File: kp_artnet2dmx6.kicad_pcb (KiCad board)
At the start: 2 copper layers, 108 parts, among them IC1 KSZ8081MNXIA-TR, IC2 M95640-RMN6P, IC3 AP2281-3WG-7, IC4 MP2331HGTL-P, J1 RJ45_Amphenol_RJMG1BD3B8K1ANR, J10 DMX, J11 DMX, J12 DMX, J14 SWD, J15 USB-B-S-RA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

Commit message: start assigning netclasses
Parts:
- IC4: footprint SamacSys:MP2331HGTLP -> Package_TO_SOT_SMD:SOT-583-8
- U1: value STM32F407VETx -> STM32F407VGT6
- moved SW1 109.0 mm to (131.7, 112.3), turned to -90 degrees
- moved R1 100.9 mm to (126.8, 113.0), turned to 0 degrees
- moved R29 87.9 mm to (121.0, 111.1), turned to -90 degrees
- moved R30 83.3 mm to (118.5, 111.1), turned to -90 degrees
- moved J14 81.6 mm to (117.6, 117.2), turned to 90 degrees
- moved R31 78.8 mm to (115.9, 111.1), turned to -90 degrees
- moved R32 74.9 mm to (113.6, 111.1), turned to -90 degrees
- moved R21 72.5 mm to (98.5, 94.8), turned to 90 degrees
- moved C3 67.7 mm to (99.5, 90.7), turned to -90 degrees
- moved C4 59.1 mm to (103.3, 74.6), turned to 0 degrees
- moved C9 58.1 mm to (103.1, 72.6), turned to 0 degrees
- moved C5 52.8 mm to (88.5, 90.7), turned to -90 degrees
- moved R19 50.5 mm to (107.3, 56.5)
- moved C21 50.5 mm to (106.5, 61.0)
- moved IC2 50.5 mm to (102.6, 58.3)
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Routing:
- added copper zone on In2.Cu, net +3.3V
- added copper zone on In2.Cu, net +5V
- added copper zone on In2.Cu, net +5V_IN
- added copper zone on B.Cu, net GND
- added copper zone on F.Cu, net GND
- added copper zone on In1.Cu, net GND
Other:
- board outline added: 84 x 104 mm
- copper layers 2 -> 4
- rule pad_to_mask_clearance: 0 -> 0.05

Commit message: main pcb : everything is connected
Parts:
- moved R21 31.7 mm to (99.4, 63.2), turned to 0 degrees
- moved R30 14.8 mm to (104.5, 115.8), turned to 90 degrees
- moved R29 14.8 mm to (107.0, 115.8), turned to 90 degrees
- moved R31 14.8 mm to (101.9, 115.8), turned to 90 degrees
- moved R32 14.8 mm to (99.7, 115.9), turned to 90 degrees
- moved J14 14.4 mm to (103.3, 116.0)
- moved R25 13.4 mm to (77.9, 35.0), turned to -45 degrees
- moved R24 11.6 mm to (75.4, 37.6), turned to -45 degrees
- moved C14 11.0 mm to (69.2, 83.2)
- moved D1 11.0 mm to (72.1, 81.7)
- moved R7 11.0 mm to (72.3, 83.2)
- moved R14 9.23 mm to (94.3, 102.9), turned to -45 degrees
- moved R19 8.43 mm to (99.1, 54.5)
- moved R13 8.07 mm to (93.1, 104.1), turned to -45 degrees
- moved C21 7.74 mm to (99.0, 59.1)
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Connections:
- net Net-(C38-Pad1) renamed /mp2331_fb2
- net Net-(C39-Pad2) renamed /mp2331_bst2
- net Net-(IC1-REXT) renamed /ksz_rext
- net Net-(IC4-BST) renamed /mp2331_bst1
- net Net-(IC4-EN) renamed /mp2331_en
- net Net-(IC4-FB) renamed /mp2331_fb1
- net Net-(IC4-PG) renamed /mp2331_pg
- net Net-(IC4-SS) renamed /mp2331_ss
- net Net-(J1-PadL1) renamed /ksz_led0+
- net Net-(J1-PadL4) renamed /ksz_led1+
- net Net-(J1-RCT) renamed /rj45_tct
- net Net-(J1-TCT) renamed /rj45_rct
- net Net-(J14-Pin_10) renamed /swd_nrst
- net Net-(J14-Pin_2) renamed /swd_io
- net Net-(J14-Pin_4) renamed /swd_clk
- net Net-(J14-Pin_6) renamed /swd_swo
- net Net-(Q1-D) renamed /usbmos1
- net Net-(Q1-S) renamed /usbmos2
- net Net-(SW1-B) renamed /bootswitch
- J1 pad R8: Earth -> GND
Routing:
- net GND: track 0.00 -> 107.1 mm, vias 0 -> 46
- net STM_NRST: track 0.00 -> 105.9 mm, vias 0 -> 6
- net +3.3V: track 0.00 -> 89.9 mm, vias 0 -> 27
- net STM_SPI2_MISO: track 0.00 -> 82.0 mm, vias 0 -> 2
- net STM_SPI2_SCK: track 0.00 -> 80.6 mm, vias 0 -> 2
- net STM_SPI2_MOSI: track 0.00 -> 76.8 mm, vias 0 -> 3
- net STM_BOOT0: track 0.00 -> 72.7 mm
- net STM_PWR_5V_EN_GPIO: track 0.00 -> 69.0 mm, vias 0 -> 2
- net STM_USB_D-: track 0.00 -> 68.0 mm, vias 0 -> 2
- net STM_SWO: track 0.00 -> 67.7 mm, vias 0 -> 2
- net STM_USB_D+: track 0.00 -> 67.4 mm, vias 0 -> 2
- net STM_MCP_RESET_GPIO: track 0.00 -> 65.6 mm, vias 0 -> 1
- net STM_MCP_INTB_GPIO: track 0.00 -> 63.1 mm, vias 0 -> 1
- net STM_I2C1_SCL: track 0.00 -> 62.6 mm, vias 0 -> 2
- net STM_I2C1_SDA: track 0.00 -> 59.8 mm, vias 0 -> 2
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- added copper zone on In2.Cu, net +5V_USB
- added copper zone on B.Cu, net Earth
- added copper zone on F.Cu, net Earth

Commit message: fix drc errors
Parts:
- removed TP1: testpoint, TestPoint:TestPoint_THTPad_1.5x1.5mm_Drill0.7mm
- moved R10 2.12 mm to (76.8, 111.2)
- moved R11 2.12 mm to (78.5, 111.2)
- moved R2 2.12 mm to (72.0, 111.2)
- moved R3 2.12 mm to (70.2, 111.3)
- moved R8 2.12 mm to (73.7, 111.2)
- moved R9 2.12 mm to (75.2, 111.2)
- moved C5 0.57 mm to (88.7, 90.2), turned to 180 degrees
- moved C16 0.25 mm to (81.3, 104.6)
- moved C17 0.25 mm to (79.7, 103.0)
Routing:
- net STM_SPI2_NSS2_GPIO: track 0.00 -> 102.1 mm, vias 0 -> 3
- net STM_ETH_TX_EN: track 0.00 -> 27.2 mm, vias 0 -> 2
- net GND: track 107.1 -> 114.9 mm, vias 46 -> 50
- net STM_ETH_RXD3: track 36.8 -> 42.3 mm
- net STM_ETH_RXD2: track 33.9 -> 39.1 mm
- net STM_ETH_RXD0: track 29.6 -> 34.0 mm
- net STM_ETH_RXD1: track 33.8 -> 36.0 mm
- net /ksz_rext: track 7.65 -> 9.77 mm
- net STM_ETH_MDIO: track 41.8 -> 43.8 mm
- net MCP_B4: track 25.6 -> 24.9 mm
- net MCP_B7: track 25.4 -> 24.8 mm
- net STM_ETH_TXD0: track 33.5 -> 34.1 mm
- net +3.3V: track 89.9 -> 90.2 mm, vias 27 -> 28
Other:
- outline, holes or cut-outs redrawn

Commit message: schematic: change connectors from jst xh to IDC
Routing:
- net GND: vias 50 -> 70
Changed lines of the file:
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@@
 	)
 	(via
+		(at 62 42)
+		(size 0.8)
+		(drill 0.25)
+		(layers "F.Cu" "B.Cu")
+		(net "GND")
+	)
+	(via
 		(at 80.55 73.95)
 		(size 0.8)
@@
 	)
 	(via
+		(at 60.5 33.5)
+		(size 0.8)
+		(drill 0.25)
+		(layers "F.Cu" "B.Cu")
+		(net "GND")
+	)
+	(via
+		(at 84 33.5)
+		(size 0.8)
+		(drill 0.25)
+		(layers "F.Cu" "B.Cu")
+		(net "GND")
+	)
+	(via
 		(at 105.55 72.65)
 		(size 0.8)
@@
 	)
 	(via
+		(at 88.5 113.5)
+		(size 0.8)
+		(drill 0.25)
+		(layers "F.Cu" "B.Cu")
+		(net "GND")
+	)
+	(via
+		(at 102.5 100)
+		(size 0.8)
+		(drill 0.25)
+		(layers "F.Cu" "B.Cu")
+		(net "GND")
+	)
+	(via
 		(at 91.4 107.35)
 		(size 0.8)
@@
 	)
 	(via
+		(at 129 39)
+		(size 0.8)
+		(drill 0.25)
+		(layers "F.Cu" "B.Cu")
+		(net "GND")
+	)
+	(via
 		(at 103.25 75.5)
 		(size 0.8)
@@
 	)
 	(via
+		(at 67.5 63.5)
+		(size 0.8)
+		(drill 0.25)
+		(layers "F.Cu" "B.Cu")
+		(net "GND")
+	)
+	(via
 		(at 80.6 80.3)
 		(size 0.8)
@@
 	)
 	(via
+		(at 94.5 123)
+		(size 0.8)
+		(drill 0.25)
+		(layers "F.Cu" "B.Cu")
+		(net "GND")
+	)
+	(via
 		(at 68.15 112.225)
 		(size 0.8)
@@
 	)
 	(via
+		(at 81 123)
+		(size 0.8)
+		(drill 0.25)
+		(layers "F.Cu" "B.Cu")
+		(net "GND")
+	)
+	(via
+		(at 68.5 123)
+		(size 0.8)
+		(drill 0.25)
+		(layers "F.Cu" "B.Cu")
+		(net "GND")
+	)
+	(via
 		(at 105.3 74.65)
 		(size 0.8)
@@
 	)
 	(via
+		(at 72 72.5)
+		(size 0.8)
+		(drill 0.25)
+		(layers "F.Cu" "B.Cu")
+		(net "GND")
+	)
+	(via
 		(at 104.53 111.99)
 		(size 0.8)
@@
 	)
 	(via
+		(at 64 72.5)
+		(size 0.8)
+		(drill 0.25)
+		(layers "F.Cu" "B.Cu")
+		(net "GND")
+	)
+	(via
 		(at 82.5 49.65)
 		(size 0.8)
@@
 	)
 	(via
+		(at 121 116.5)
+		(size 0.8)
+		(drill 0.25)
+		(layers "F.Cu" "B.Cu")
+		(net "GND")
+	)
+	(via
+		(at 87 63)
+		(size 0.8)
+		(drill 0.25)
+		(layers "F.Cu" "B.Cu")
+		(net "GND")
+	)
+	(via
 		(at 79.6 104.65)
 		(size 0.8)
@@
 	)
 	(via
+		(at 79.5 44)
+		(size 0.8)
+		(drill 0.25)
+		(layers "F.Cu" "B.Cu")
+		(net "GND")
+	)
+	(via
+		(at 107 61)
+		(size 0.8)
+		(drill 0.25)
+		(layers "F.Cu" "B.Cu")
+		(net "GND")
+	)
+	(via
 		(at 82.2 87.4)
 		(size 0.8)
@@
 	)
 	(via
+		(at 112 99)
+		(size 0.8)
+		(drill 0.25)
+		(layers "F.Cu" "B.Cu")
+		(net "GND")
+	)
+	(via
 		(at 76.65 101.2)
 		(size 0.8)
@@
 	)
 	(via
+		(at 106 54)
+		(size 0.8)
+		(drill 0.25)
+		(layers "F.Cu" "B.Cu")
+		(net "GND")
+	)
+	(via
 		(at 59.5 99.25)
 		(size 0.8)
@@
 	)
 	(via
+		(at 64 83)
+		(size 0.8)
+		(drill 0.25)
+		(layers "F.Cu" "B.Cu")
+		(net "GND")
+	)
+	(via
 		(at 88.374694 86.224694)
 		(size 0.8)
@@
 	)
 	(via
+		(at 115 122.5)
+		(size 0.8)
+		(drill 0.25)
+		(layers "F.Cu" "B.Cu")
+		(net "GND")
+	)
+	(via
 		(at 100.63 111.79)
 		(size 0.8)
@@
 		)
 		(min_thickness 0.25)
-		(fill yes
+		(fill
 			(thermal_gap 0.5)
 			(thermal_bridge_width 0.5)
@@
 		)
 		(min_thickness 0.25)
-		(fill yes
+		(fill
 			(thermal_gap 0.5)
 			(thermal_bridge_width 0.5)
@@
 		)
 		(min_thickness 0.25)
-		(fill yes
+		(fill
 			(thermal_gap 0.5)
 			(thermal_bridge_width 0.5)
@@
 		)
 		(min_thickness 0.25)
-		(fill yes
+		(fill
 			(thermal_gap 0.5)
 			(thermal_bridge_width 0.5)
@@
 		)
 		(min_thickness 0.25)
-		(fill yes
+		(fill
 			(thermal_gap 0.5)
 			(thermal_bridge_width 0.5)
@@
 		)
 		(min_thickness 0.25)
-		(fill yes
+		(fill
 			(thermal_gap 0.5)
 			(thermal_bridge_width 0.5)
@@
 		)
 		(min_thickness 0.25)
-		(fill yes
+		(fill
 			(thermal_gap 0.5)
 			(thermal_bridge_width 0.5)
@@
 		)
 		(min_thickness 0.25)
-		(fill yes
+		(fill
 			(thermal_gap 0.5)
 			(thermal_bridge_width 0.5)
@@
 		)
 		(min_thickness 0.25)
-		(fill yes
+		(fill
 			(thermal_gap 0.5)
 			(thermal_bridge_width 0.5)
@@
 		)
 		(min_thickness 0.25)
-		(fill yes
+		(fill
 			(thermal_gap 0.5)
 			(thermal_bridge_width 0.5)
@@
 		)
 		(min_thickness 0.25)
-		(fill yes
+		(fill
 			(thermal_gap 0.5)
 			(thermal_bridge_width 0.5)

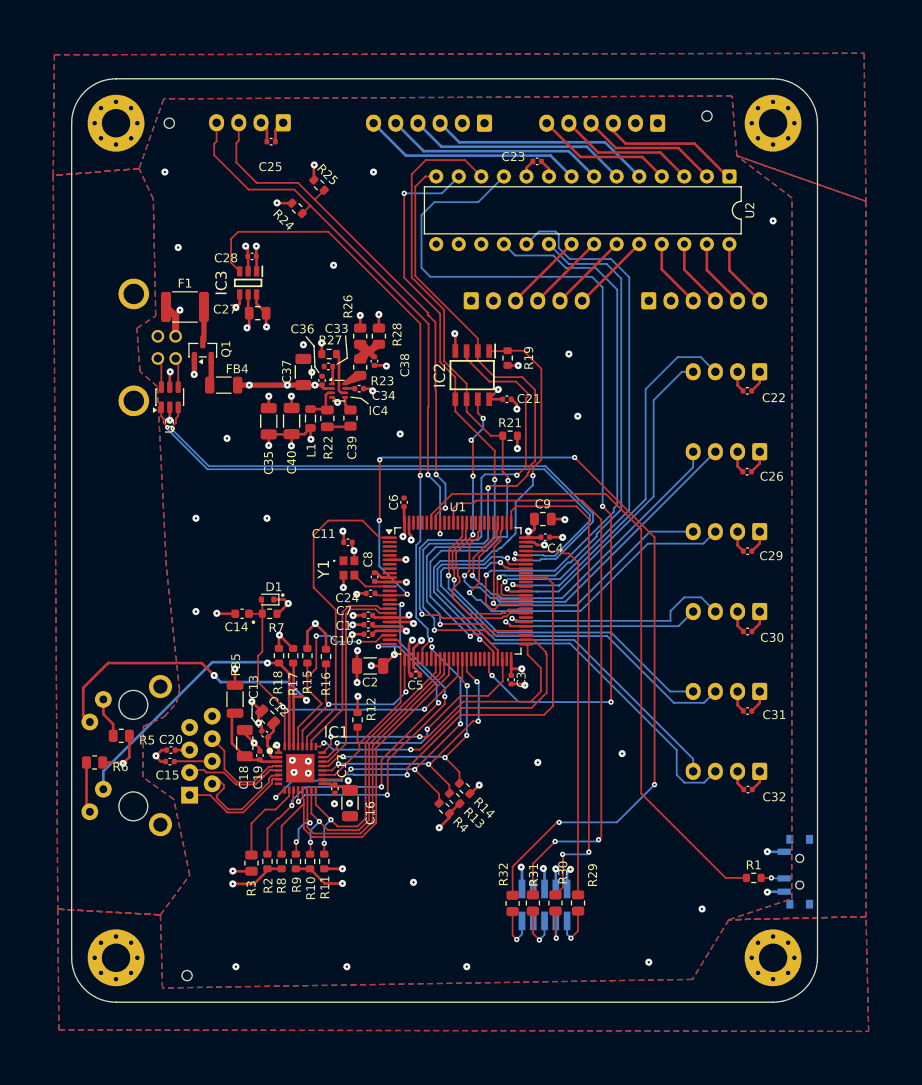
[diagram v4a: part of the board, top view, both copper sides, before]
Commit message: pcb: change connectors to IDC
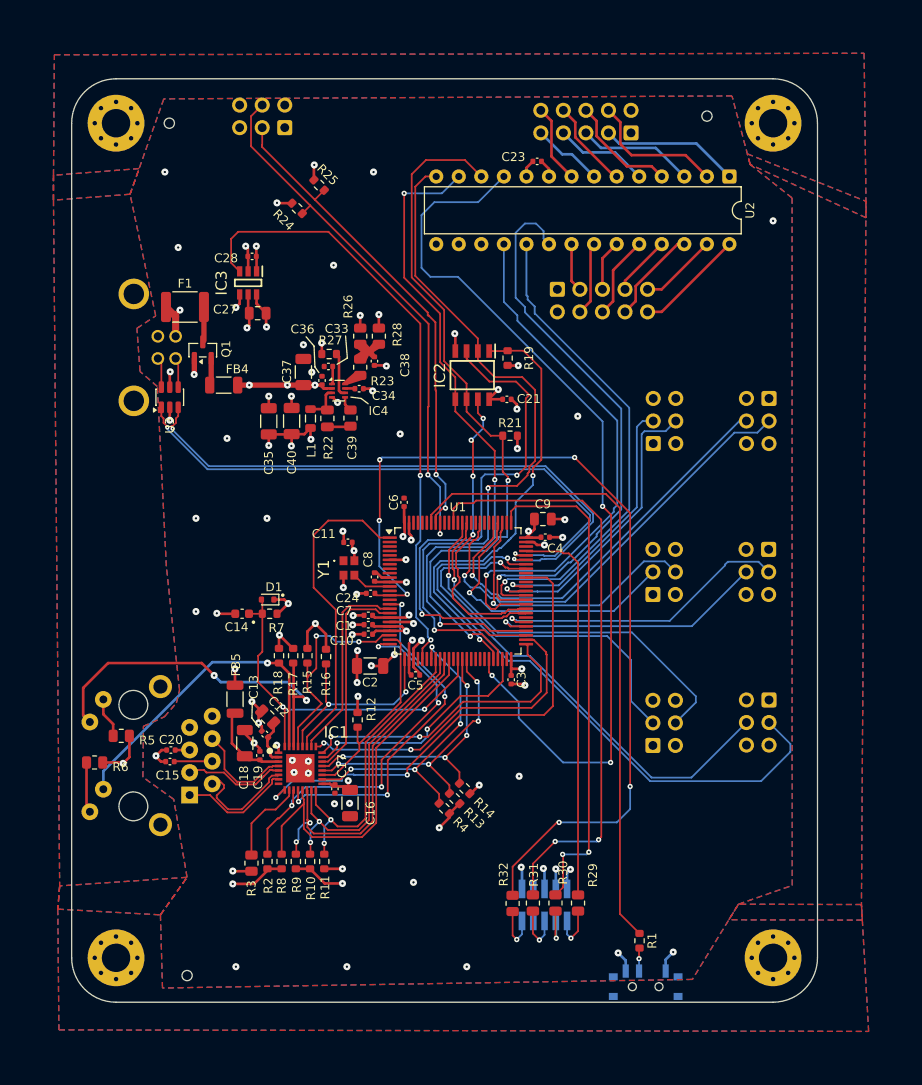
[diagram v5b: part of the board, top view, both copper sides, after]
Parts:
- removed C22, C25, C26, C29, C30, C31, C32: 100n, Capacitor_SMD:C_0402_1005Metric
- removed J4, J6: BTN, Connector_JST:JST_XH_B6B-XH-A_1x06_P2.50mm_Vertical
- J10, J11, J12, J2, J7, J8, J9: footprint Connector_JST:JST_XH_B4B-XH-A_1x04_P2.50mm_Vertical -> Connector_IDC:IDC-Header_2x03_P2.54mm_Vertical
- J3, J5: footprint Connector_JST:JST_XH_B6B-XH-A_1x06_P2.50mm_Vertical -> Connector_IDC:IDC-Header_2x05_P2.54mm_Vertical
- moved SW1 21.2 mm to (114.7, 124.9), turned to 180 degrees
- moved R1 14.7 mm to (114.0, 120.1), turned to -90 degrees
- moved J12 14.5 mm to (115.5, 64.1), turned to 0 degrees
- moved J10 14.0 mm to (115.5, 81.1), turned to 0 degrees
- moved J8 13.5 mm to (115.5, 98.1), turned to 0 degrees
- moved J5 9.79 mm to (104.7, 46.7), turned to -90 degrees
- moved J7 8.11 mm to (128.5, 93.0)
- moved J9 7.07 mm to (128.5, 76.0)
- moved J11 6.09 mm to (128.5, 59.0)
- moved J3 3.19 mm to (113.0, 29.1), turned to 90 degrees
- moved J2 0.58 mm to (74.0, 28.5), turned to 90 degrees
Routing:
- net GND: track 114.9 -> 97.7 mm, vias 70 -> 66
- net +5V: track 23.4 -> 6.24 mm
- net MCP_B6: track 24.8 -> 8.03 mm
- net MCP_B7: track 24.8 -> 8.88 mm
- net MCP_B5: track 24.9 -> 10.1 mm
- net MCP_B4: track 24.9 -> 10.6 mm
- net STM_USART6_RX: track 43.1 -> 30.4 mm
- net STM_USART1_RX: track 56.0 -> 67.8 mm
- net STM_UART4_RX: track 41.4 -> 32.5 mm
- net STM_USART1_TX: track 49.9 -> 58.0 mm
- net STM_USART3_TX: track 24.5 -> 32.3 mm
- net STM_UART5_RX: track 43.7 -> 51.2 mm
- net STM_USART3_RX: track 27.2 -> 34.0 mm
- net STM_MCP_INTB_GPIO: track 63.1 -> 56.5 mm
- net STM_UART5_TX: track 40.7 -> 47.1 mm
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
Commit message: dmxinout: do board
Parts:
- added G***: LOGO, homemade_footprints:pxm_testlogo_v1, F.Cu at (120.2, 111.3)
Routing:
- net +5V_IN: vias 6 -> 7
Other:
- board text added: "JLCJLCJLCJLC"
- board text added: "artnet2dmx6_00"

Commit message: main board : start doing sig gnd gnd sigpow
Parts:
- IC4: footprint Package_TO_SOT_SMD:SOT-583-8 -> SamacSys:MP2331HGTLP
- moved U2 70.8 mm to (130.3, 104.5), turned to 180 degrees
- moved J8 69.3 mm to (89.0, 34.0)
- moved J5 64.7 mm to (140.0, 100.9), turned to 180 degrees
- moved J3 59.7 mm to (137.5, 83.5), turned to 0 degrees
- moved C23 58.6 mm to (132.2, 82.8), turned to 90 degrees
- moved J10 48.7 mm to (103.0, 34.0)
- moved IC2 46.1 mm to (115.7, 97.7), turned to 90 degrees
- moved R19 44.0 mm to (110.7, 96.9), turned to -90 degrees
- moved J7 43.6 mm to (110.0, 53.5), turned to 0 degrees
- moved C21 39.4 mm to (112.2, 96.2), turned to -90 degrees
- moved G*** 35.8 mm to (85.5, 120.0), turned to 0 degrees
- moved J11 33.0 mm to (96.0, 53.6), turned to 0 degrees
- moved R21 31.3 mm to (115.1, 90.3), turned to 180 degrees
- moved J12 30.1 mm to (117.0, 34.0)
- moved C2 27.6 mm to (105.5, 72.3), turned to 0 degrees
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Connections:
- J10 pad 3: STM_UART4_RX -> GND
- J10 pad 4: STM_UART4_TX -> STM_UART4_RX
- J10 pad 5: unconnected-(J10-Pin_5-Pad5) -> GND
- J10 pad 6: unconnected-(J10-Pin_6-Pad6) -> STM_UART4_TX
- J11 pad 3: STM_UART5_RX -> GND
- J11 pad 4: STM_UART5_TX -> STM_UART5_RX
- J11 pad 5: unconnected-(J11-Pin_5-Pad5) -> GND
- J11 pad 6: unconnected-(J11-Pin_6-Pad6) -> STM_UART5_TX
- J12 pad 3: STM_USART6_RX -> GND
- J12 pad 4: STM_USART6_TX -> STM_USART6_RX
- J12 pad 5: unconnected-(J12-Pin_5-Pad5) -> GND
- J12 pad 6: unconnected-(J12-Pin_6-Pad6) -> STM_USART6_TX
- J2 pad 3: STM_I2C1_SDA -> GND
- J2 pad 4: STM_I2C1_SCL -> STM_I2C1_SDA
- J2 pad 5: unconnected-(J2-Pin_5-Pad5) -> GND
- J2 pad 6: unconnected-(J2-Pin_6-Pad6) -> STM_I2C1_SCL
- J7 pad 3: STM_USART1_RX -> GND
- J7 pad 4: STM_USART1_TX -> STM_USART1_RX
- J7 pad 5: unconnected-(J7-Pin_5-Pad5) -> GND
- J7 pad 6: unconnected-(J7-Pin_6-Pad6) -> STM_USART1_TX
- J8 pad 3: STM_USART2_RX -> GND
- J8 pad 4: STM_USART2_TX -> STM_USART2_RX
- J8 pad 5: unconnected-(J8-Pin_5-Pad5) -> GND
- J8 pad 6: unconnected-(J8-Pin_6-Pad6) -> STM_USART2_TX
- J9 pad 3: STM_USART3_RX -> GND
- J9 pad 4: STM_USART3_TX -> STM_USART3_RX
- J9 pad 5: unconnected-(J9-Pin_5-Pad5) -> GND
- J9 pad 6: unconnected-(J9-Pin_6-Pad6) -> STM_USART3_TX
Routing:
- net STM_SPI2_NSS2_GPIO: track 103.9 -> 46.5 mm, vias 3 -> 2
- net MCP_A0: track 5.48 -> 56.3 mm
- net STM_NRST: track 103.7 -> 54.9 mm, vias 6 -> 2
- net MCP_A2: track 5.75 -> 46.5 mm
- net STM_MCP_RESET_GPIO: track 61.1 -> 23.4 mm, vias 1 -> 2
- net STM_MCP_INTA_GPIO: track 64.5 -> 29.4 mm
- net STM_USART1_RX: track 67.8 -> 33.8 mm, vias 1 -> 0
- net +3.3V: track 90.6 -> 120.4 mm, vias 28 -> 24
- net MCP_A4: track 6.80 -> 36.5 mm
- net STM_USART6_RX: track 30.4 -> 58.0 mm, vias 1 -> 0
- net STM_UART5_RX: track 51.2 -> 23.7 mm, vias 1 -> 0
- net STM_USART6_TX: track 34.2 -> 61.5 mm, vias 1 -> 0
- net STM_MCP_INTB_GPIO: track 56.5 -> 29.2 mm
- net STM_SPI2_NSS1_GPIO: track 50.5 -> 24.0 mm, vias 2 -> 0
- net GND: track 97.7 -> 122.7 mm, vias 66 -> 40
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- added copper zone on B.Cu, net +3.3V
- added copper zone on B.Cu, net +5V
- added copper zone on In2.Cu, net GND
- removed copper zone on In2.Cu, net +3.3V
- removed copper zone on In2.Cu, net +5V
- removed copper zone on In2.Cu, net +5V_IN
- removed copper zone on In2.Cu, net +5V_USB
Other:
- board size 84 x 104 mm -> 95 x 104 mm
- board text added: "BTN_A"
- board text added: "BTN_B"
- board text added: "DMX1"
- board text added: "DMX2"
- board text added: "DMX3"
- board text added: "DMX4"
- board text added: "DMX5"
- board text added: "DMX6"
- board text added: "SCREEN"
